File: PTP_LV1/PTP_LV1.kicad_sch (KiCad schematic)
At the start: 2 parts

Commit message: LV2 Riješen
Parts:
- added C1: 222u, symbol Device:C_Polarized_Small
- added C3: 22u, symbol Device:C_Polarized_Small
- added C4: 1u, symbol Device:C
- added C7: 10u, symbol Device:C
- added C8: 100n, symbol Device:C
- added D1: 11DQ06, symbol Device:D_Schottky_Small_Filled
- added D2, D3, D4, D5: (no value), symbol Device:LED
- added J1: ~, symbol Connector:Screw_Terminal_01x02
- added L1: 330u, symbol Device:L
- added R3, R4: 47k, symbol Device:R_Small
- added R6, R7, R8, R9: 4k7, symbol Device:R_Small
- added SW1: ~, symbol Switch:SW_Push
- added SW2: ~, symbol Switch:SW_SPDT
- added U2: LM2574N-5, Package_DIP:DIP-8_W7.62mm, symbol Regulator_Switching:LM2574N-5
- added U5: NE555P, Package_DIP:DIP-8_W7.62mm, symbol Timer:NE555P
- R1, R2: value R_Small -> 2k
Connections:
- net GND: now also C1.2, C3.2, C4.1, C7.2, C8.2, D1.2 (A), J1.2 (Pin_2), R6.2, R7.2, R8.2, R9.2, SW1.1, U2.2 (SGND), U2.3 (~{ON}/OFF), U2.4 (PGND), U5.1 (GND); no longer R2.1
- net +3.3V renamed +5V
- net +5V: now also C1.1, C8.1, L1.2, R3.1, U2.1 (FB), U5.4 (R), U5.8 (VCC)
- net U_izlaz: no longer names the net of R1.2, R2.2
- net U_izlaz: now also C4.2, SW2.3 (A)
- new net: R2.1, SW1.2
- new net: D3.1 (K), R7.1
- new net: D5.1 (K), R9.1
- new net: D1.1 (K), L1.1, U2.7 (OUT)
- new net: D2.1 (K), R6.1
- new net: C7.1, R4.2, U5.2 (TR), U5.6 (THR)
- new net: R3.2, R4.1, U5.7 (DIS)
- new net: D4.1 (K), R8.1
- new net 555: SW2.2 (C), U5.3 (Q)
- new net Clock: SW2.1 (B)
- new net Q0: D2.2 (A)
- new net Q1: D3.2 (A)
- new net Q2: D4.2 (A)
- new net Q3: D5.2 (A)
- new net VD: C3.1, J1.1 (Pin_1), U2.5 (VIN)

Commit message: LV3
LV3 Dovršen
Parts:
- added U6: SN74LVC1G11, SOT-23-6:SOT-23-6, symbol SN74LVC1G11:SN74LVC1G11
- C2: renamed from C1; value 222u -> 220u
- D1: renamed from D2; value (none) -> ~
- D2: renamed from D3; value (none) -> ~
- D3: renamed from D4; value (none) -> ~
- D5: value (none) -> ~
- R7: renamed from R1; value 2k -> 10k
- renumbered C3 to C1, C4 to C3, C8 to C4, C7 to C5, D1 to D4, R6 to R1, R2 to R13, R3 to R19, R7 to R2, R4 to R20, R8 to R3, R9 to R4, U2 to U1, U5 to U7
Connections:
- net +5V: now also U6.5 (VCC)
- net Clock: now also R7.2, U6.6 (C)
- net GND: now also U6.2 (GND)
- net Q1: now also U6.1 (A)
- net Q3: now also U6.3 (B)
- net at C3.2, R13.2, SW2.3 (A): no longer R7.2
- new net Reset: U6.4 (Output)
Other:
- moved on the sheet: C1, C2, D1, D2, D3, D4, D5, J1, L1, R1, R2, R3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

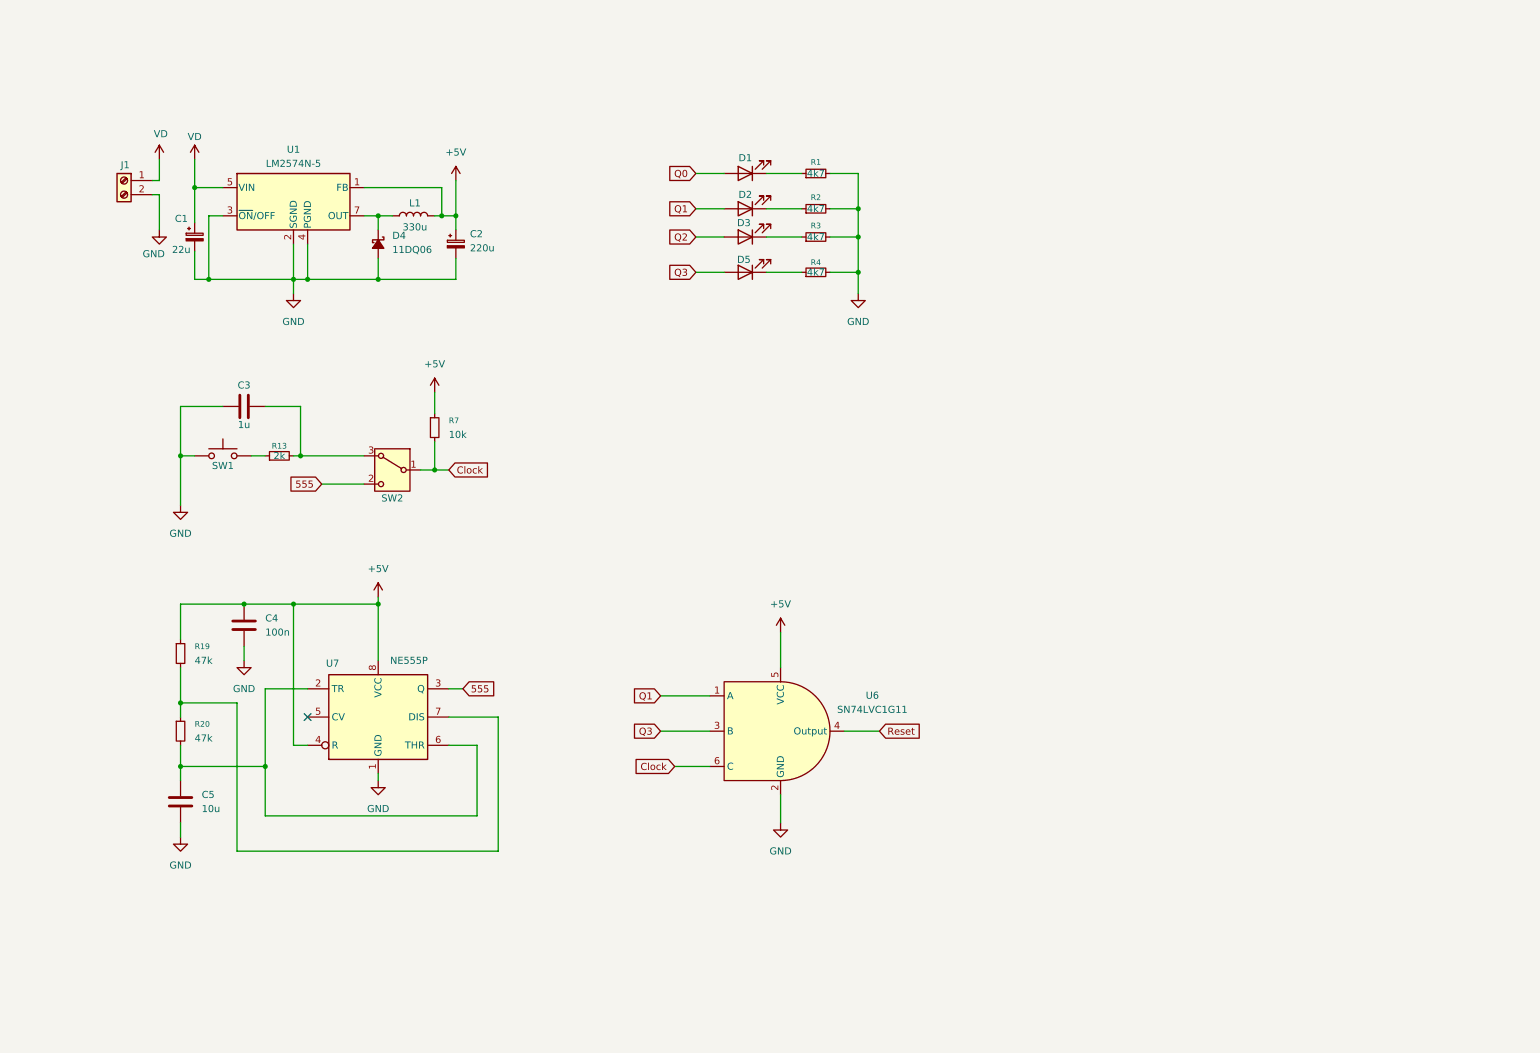
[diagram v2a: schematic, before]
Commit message: LV4
Zavrsili schemu i dodali neke footprinte (ostatak dodati doma)
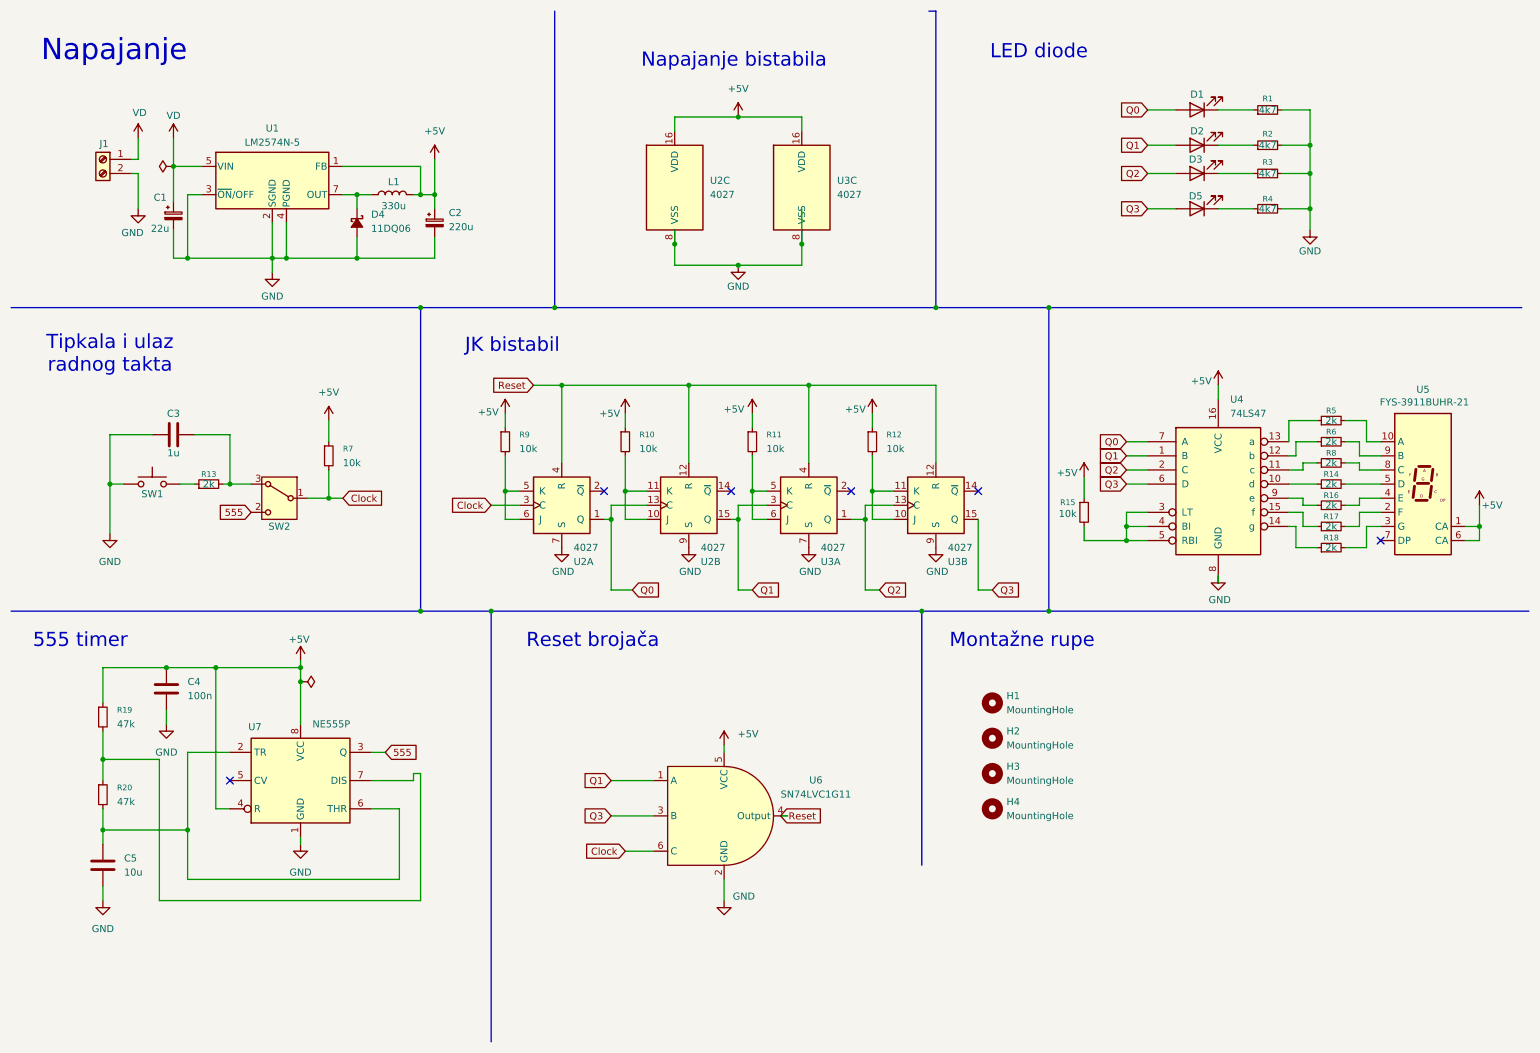
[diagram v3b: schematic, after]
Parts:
- added H1, H2, H3, H4: MountingHole, MountingHole:MountingHole_5.5mm, symbol Mechanical:MountingHole
- added R10, R11, R12, R15, R9: 10k, symbol Device:R_Small
- added R14, R16, R17, R18, R5, R6, R8: 2k, symbol Device:R_Small
- added U2, U3: 4027, symbol 4xxx:4027
- added U4: 74LS47, symbol 74xx:74LS47
- added U5: FYS-3911BUHR-21, Display_7Segment:HDSP-7401, symbol Display_Character:HDSP-7401
- C1: footprint (none) -> Capacitor_THT:CP_Radial_D5.0mm_P2.00mm; Manufacturer (none) -> AISHI; Manufacturer part number (none) -> EWH1EM220D11OT
- C2: footprint (none) -> Capacitor_THT:CP_Radial_D5.0mm_P2.00mm; Manufacturer (none) -> SAMWHA; Manufacturer part number (none) -> RD1A227M05011BB
- C3: footprint (none) -> Capacitor_SMD:C_1206_3216Metric_Pad1.33x1.80mm_HandSolder; Manufacturer (none) -> SAMSUNG; Manufacturer part number (none) -> CL31B105KBHNNNE
- C4: footprint (none) -> Capacitor_SMD:C_1206_3216Metric_Pad1.33x1.80mm_HandSolder; Manufacturer (none) -> SAMSUNG; Manufacturer part number (none) -> CL31B104KBCNNNC
- C5: footprint (none) -> Capacitor_SMD:C_1206_3216Metric_Pad1.33x1.80mm_HandSolder; Manufacturer (none) -> SAMSUNG; Manufacturer part number (none) -> CL31A106KBHNNNE
- D1, D2, D3, D5: footprint (none) -> LED_THT:LED_D5.0mm
- D4: footprint (none) -> Diode_THT:D_DO-41_SOD81_P12.70mm_Horizontal; Manufacturer (none) -> SMC DIODE SOLUTIONS; Manufacturer part number (none) -> 11DQ06TA
- J1: footprint (none) -> TerminalBlock_MetzConnect:TerminalBlock_MetzConnect_Type011_RT05502HBLC_1x02_P5.00mm_Horizontal
- U1: footprint Package_DIP:DIP-8_W7.62mm -> Package_DIP:DIP-8_W7.62mm_Socket_LongPads; Manufacturer (none) -> ONSEMI; Manufacturer part number (none) -> LM2574N-5G
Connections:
- net +5V: now also R10.1, R11.1, R12.1, R15.1, R9.1, U2.16 (VDD), U3.16 (VDD), U4.16 (VCC), U5.1 (CA), U5.6 (CA)
- net Clock: now also U2.3 (C)
- net GND: now also U2.7 (S), U2.8 (VSS), U2.9 (S), U3.7 (S), U3.8 (VSS), U3.9 (S), U4.8 (GND)
- net Q0: now also U2.1 (Q), U2.13 (C), U4.7 (A)
- net Q1: now also U2.15 (Q), U3.3 (C), U4.1 (B)
- net Q2: now also U3.1 (Q), U3.13 (C), U4.2 (C)
- net Q3: now also U3.15 (Q), U4.6 (D)
- net Reset: now also U2.12 (R), U2.4 (R), U3.12 (R), U3.4 (R)
- new net: R11.2, U3.5 (K), U3.6 (J)
- new net: R9.2, U2.5 (K), U2.6 (J)
- new net: R10.2, U2.10 (J), U2.11 (K)
- new net: R14.1, U4.10 (d)
- new net: R8.1, U4.11 (c)
- new net: R6.1, U4.12 (b)
- new net: R5.1, U4.13 (a)
- new net: R18.1, U4.14 (g)
- new net: R17.1, U4.15 (f)
- new net: R15.2, U4.3 (LT), U4.4 (BI), U4.5 (RBI)
- new net: R16.1, U4.9 (e)
- new net: R5.2, U5.10 (A)
- new net: R16.2, U5.4 (E)
- new net: R18.2, U5.3 (G)
- new net: R14.2, U5.5 (D)
- new net: R12.2, U3.10 (J), U3.11 (K)
- new net: R17.2, U5.2 (F)
- new net: R8.2, U5.8 (C)
- new net: R6.2, U5.9 (B)
- no-connect marks 1 -> 6
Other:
- note added: "555 timer"
- note added: "JK bistabil"
- note added: "LED diode"
- note added: "Montažne rupe"
- note added: "Napajanje"
- note added: "Napajanje bistabila"
- note added: "Reset brojača"
- note added: "Tipkala i ulaz radnog takta"
- moved on the sheet: C1, C2, C3, C4, C5, D1, D2, D3, D4, D5, J1, L1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

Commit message: Dovrsia footprintove eli
E to
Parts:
- J1: Manufacturer (none) -> DEGSON ELECTRONICS; Manufacturer part Number (none) -> DG301-5.0-02P-12-00A(H)
- L1: footprint (none) -> Inductor_THT:L_Radial_D7.2mm_P3.00mm_Murata_1700; Manufacturer (none) -> FERROCORE; Manufacturer Part Number (none) -> COIL0608-0.33
- R1, R2, R3, R4: footprint (none) -> Resistor_THT:R_Axial_DIN0207_L6.3mm_D2.5mm_P10.16mm_Horizontal
- R10, R11, R12, R15, R7, R9: footprint (none) -> Resistor_SMD:R_1206_3216Metric_Pad1.30x1.75mm_HandSolder
- R14, R8: footprint (none) -> Resistor_SMD:R_1206_3216Metric_Pad1.30x1.75mm_HandSolder; Manufacturer (none) -> ROYALOHM; Manufacturer Part Number (none) -> 1206S4F2001T5E
- R16, R17, R5: footprint (none) -> Resistor_SMD:R_1206_3216Metric_Pad1.30x1.75mm_HandSolder; Manufacturer (none) -> ROYALOHM; Manufacturer part Number (none) -> 1206S4F2001T5E
- R18, R6: footprint (none) -> Resistor_SMD:R_1206_3216Metric_Pad1.30x1.75mm_HandSolder; Manufacturer (none) -> ROYALOHM; Manufacturer part number (none) -> 1206S4F2001T5E
- R19, R20: footprint (none) -> Resistor_SMD:R_1206_3216Metric_Pad1.30x1.75mm_HandSolder; Manufacturer (none) -> ROYALOHM; Manufacturer part Number (none) -> 1206S4J0473T5E
- SW1: footprint (none) -> Button_Switch_THT:SW_PUSH_6mm_H4.3mm; Manufacturer (none) -> microswitch TACT; Manufacturer part number (none) -> TACT-64N-F
- SW2: footprint (none) -> Button_Switch_THT:SW_Slide_SPDT_Straight_CK_OS102011MS2Q; Manufacturer (none) -> C&K; Manufacturer Part Number (none) -> OS102011MS2QN1C
- U2, U3: footprint (none) -> Package_DIP:DIP-16_W7.62mm_Socket_LongPads; Manufacturer (none) -> RENESAS; Manufacturer part number (none) -> CD4027BMS
- U4: footprint (none) -> Package_DIP:DIP-16_W7.62mm_Socket_LongPads; Manufacturer (none) -> TEXAS INSTRUMENTS; Manufacturer Part Number (none) -> SN74LS47N
- U5: Manufacturer (none) -> FORYARD; Manufacturer Part Number (none) -> FYS-3911BUHR-21
- U6: Manufacturer (none) -> TEXAS INSTRUMENTS; Manufacturer Part Numbert (none) -> SN74LVC1G11DBVR
- U7: Manufacturer (none) -> TEXAS INSTRUMENTS; Manufacturer Part Number (none) -> NE555P
